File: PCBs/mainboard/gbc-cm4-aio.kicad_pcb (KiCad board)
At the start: 4 copper layers, 70.1 x 122.2 mm, 128 parts, among them J1 Conn_01x40, J2 AudioJack2_Ground_Switch, J4 DM3D-SF, J6 Conn_01x11, J7 Conn_01x02, P1 USB_C_Plug_USB2.0, Q1 AO4407C, Q3 2N7002E, SW1 SW_Push, SW3 SW_Push_Dual_x2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

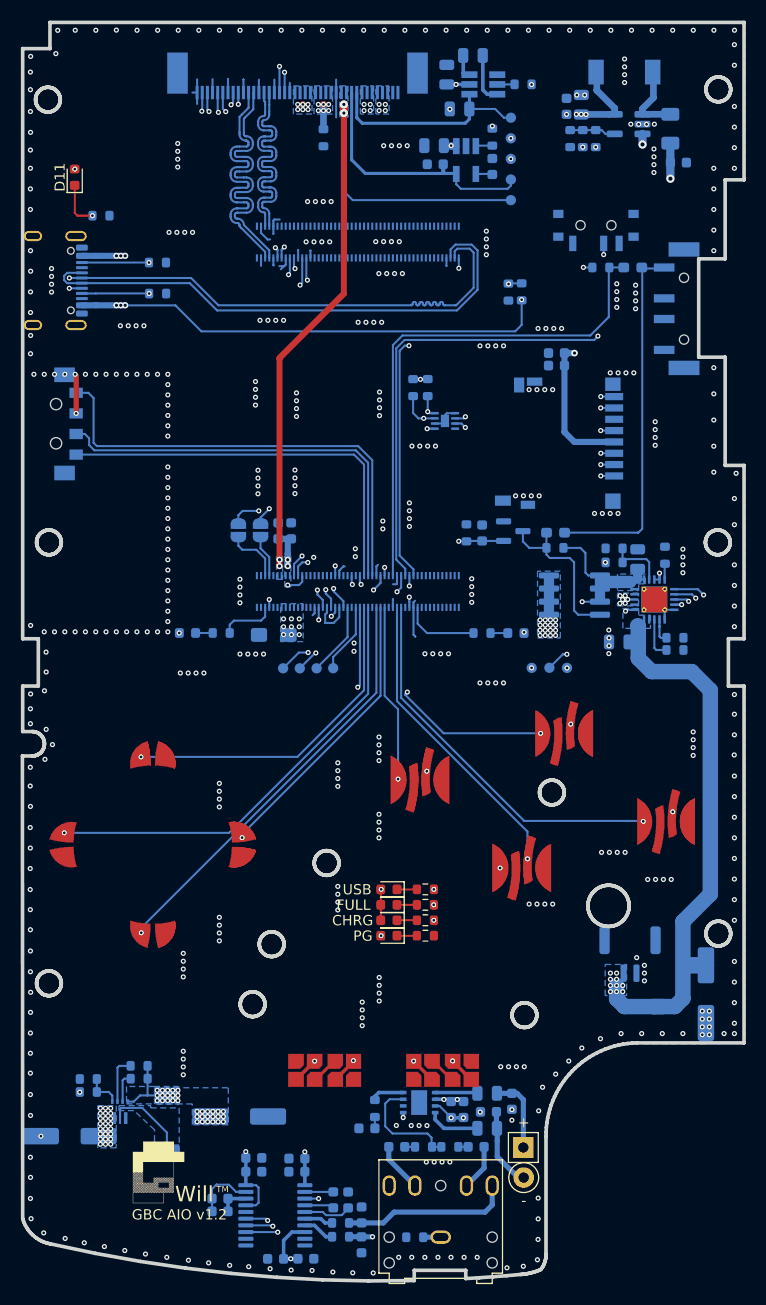
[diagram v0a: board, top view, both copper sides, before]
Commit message: move i2c bus to i2c1
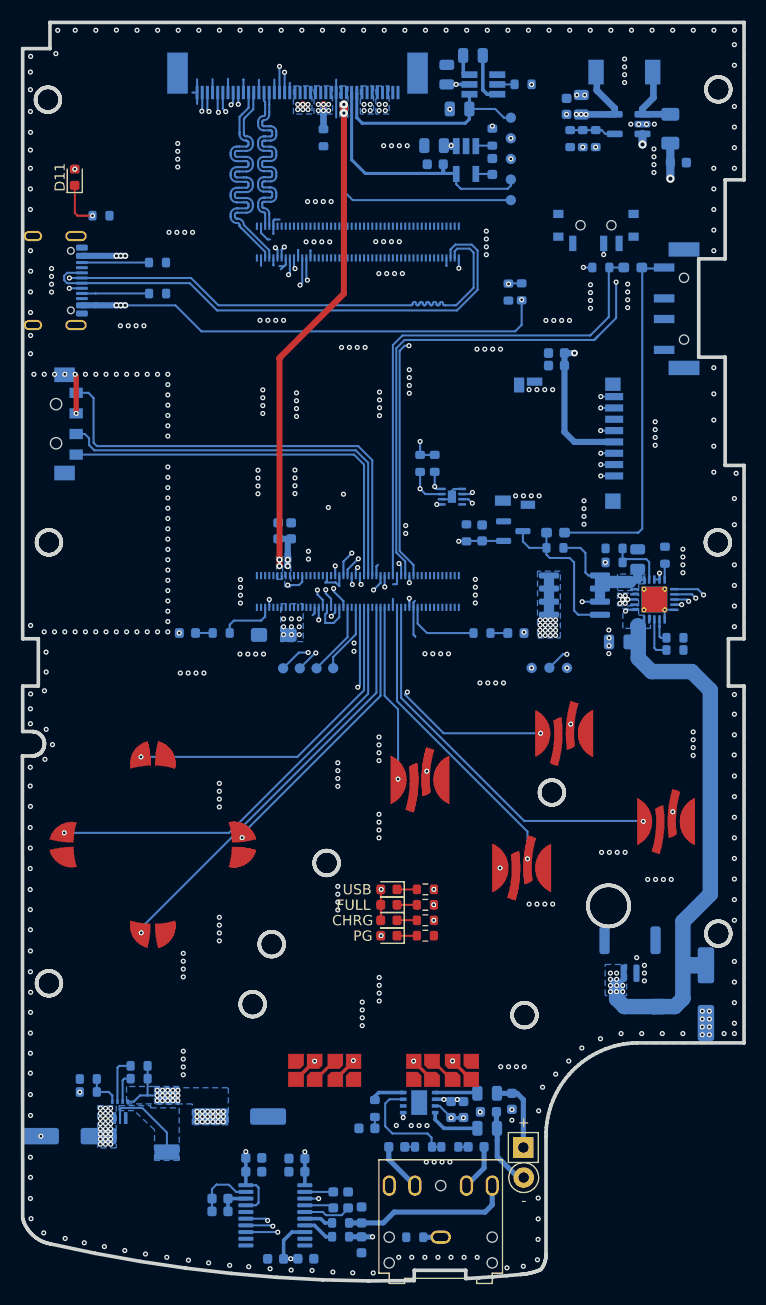
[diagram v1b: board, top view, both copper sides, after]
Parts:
- removed the ? at (151.1, 248.5)
- removed JP1, JP2: ~, Jumper:SolderJumper-2_P1.3mm_Open_RoundedPad1.0x1.5mm
- moved R1 7.38 mm to (178.9, 178.6)
- moved R2 7.38 mm to (177.5, 178.6)
- moved U4 7.38 mm to (180.6, 181.9)
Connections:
- Module1 pad 56: unconnected-(Module1A-GPIO3-Pad56) -> /SCL1
- Module1 pad 58: unconnected-(Module1A-GPIO2-Pad58) -> /SDA1
- R1 pad 2: /SDA0 -> /SDA1
- R2 pad 2: /SCL0 -> /SCL1
- SCL1 pad 1: /SCL0 -> /SCL1
- SDA1 pad 1: /SDA0 -> /SDA1
- U4 pad 7: /SCL0 -> /SCL1
- U4 pad 8: /SDA0 -> /SDA1
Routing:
- net /SDA0: track 37.0 -> 0.00 mm, vias 3 -> 0
- net /SCL0: track 36.0 -> 0.00 mm, vias 3 -> 0
- net /IP1: track 38.2 -> 6.51 mm, vias 2 -> 0
- net /IP0: track 38.2 -> 6.51 mm, vias 2 -> 0
- net /SDA1: track 0.00 -> 31.1 mm, vias 0 -> 3
- net /SCL1: track 0.00 -> 28.7 mm, vias 0 -> 3
- net /ALERT: track 31.3 -> 10.8 mm, vias 3 -> 2
- net +BATT: track 88.9 -> 81.3 mm
- net unconnected-(Module1A-AnalogIP0-Pad96): track 5.62 -> 0.00 mm
- net unconnected-(Module1A-AnalogIP1-Pad94): track 4.10 -> 0.00 mm
- net GND: track 54.3 -> 57.3 mm, vias 463 -> 458
- net /RPI_BOOT: track 58.2 -> 60.9 mm
- net /BL_PWM: track 61.0 -> 63.0 mm
- net /PWR_ON: track 14.6 -> 16.4 mm
- net VBUS: track 223.1 -> 221.5 mm
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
